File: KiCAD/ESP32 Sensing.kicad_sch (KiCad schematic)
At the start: 33 parts, among them J2 Ext Battery 3.3V, J3 Sensor, J4 Thermistor, J5 Light Detect, J6 MICRO-B USB, Q1 MMBT3904, Q2 NDS356AP, SW1 PTS526_SK15_SMTR2_LFS, U1 ESP32-WROOM-32, U2 AMS1117-3.3

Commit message: Documentation update
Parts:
- R13: footprint (none) -> Resistor_SMD:R_0805_2012Metric_Pad1.20x1.40mm_HandSolder
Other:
- note added: "Generic Sensor Input"
- note added: "Heat Sensor"
- note added: "Light Sensor"
- note added: "Voltage Monitoring"
- note removed: "Battery Voltage Monitoring"
- note removed: "Light Detector"
- note removed: "Sensor Input"
- note removed: "Thermistor"
- company: (none) -> Guy Turcotte
- title: (none) -> ESP32 Sensing Device
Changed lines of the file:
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@@
 (kicad_sch (version 20211123) (generator eeschema)
   (paper "A4")
+  (title_block
+    (title "ESP32 Sensing Device")
+    (date "2022-03-23")
+    (rev "1.0")
+    (company "Guy Turcotte")
+  )
   (junction (at 49.53 109.22) (diameter 0) (color 0 0 0 0)
   )
@@
     (stroke (width 0) (type default) (color 0 0 0 0))
   )
-  (text "Thermistor" (at 26.67 153.67 0)
+  (text "Heat Sensor" (at 26.67 153.67 0)
     (effects (font (size 1.27 1.27)) (justify left bottom))
   )
-  (text "Battery Voltage Monitoring" (at 185.42 86.36 0)
+  (text "Voltage Monitoring" (at 185.42 86.36 0)
     (effects (font (size 1.27 1.27)) (justify left bottom))
   )
@@
     (effects (font (size 1.27 1.27)) (justify left bottom))
   )
-  (text "Sensor Input" (at 185.42 35.56 0)
+  (text "Generic Sensor Input" (at 185.42 35.56 0)
     (effects (font (size 1.27 1.27)) (justify left bottom))
   )
@@
     (effects (font (size 1.27 1.27)) (justify left bottom))
   )
-  (text "Light Detector" (at 68.58 153.67 0)
+  (text "Light Sensor" (at 68.58 153.67 0)
     (effects (font (size 1.27 1.27)) (justify left bottom))
   )
@@
       (effects (font (size 1.27 1.27)) (justify left))
     )
-    (property "Footprint" "" (id 2) (at 50.292 68.58 90)
-      (effects (font (size 1.27 1.27)) hide)
-    )
+    (property "Footprint" "Resistor_SMD:R_0805_2012Metric_Pad1.20x1.40mm_HandSolder" (id 2) (at 50.292 68.58 90)
+      (effects (font (size 1.27 1.27)) hide)
+    )

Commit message: Some symbol adjustments
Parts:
- removed Q2: NDS356AP, Package_TO_SOT_SMD:SOT-23, symbol Transistor_FET:BSS84
- added Q2: (no value), Package_TO_SOT_SMD:SOT-23, symbol ESP32 Sensing:NDS356AP
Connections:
- net +3V3: now also Q2.2 (S)
- net at Q1.3 (C), R1.2: now also Q2.1 (G)
- net at R3.2: now also Q2.3 (D)
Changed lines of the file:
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@@
     (pin "2")
-  )
-  (symbol (lib_id "Transistor_FET:BSS84") (at 217.17 102.87 270) (mirror x) (unit 1)
-    (in_bom yes) (on_board yes) (fields_autoplaced)
-    (property "Reference" "Q2" (id 0) (at 217.17 92.71 90))
-    (property "Value" "NDS356AP" (id 1) (at 217.17 95.25 90))
-    (property "Footprint" "Package_TO_SOT_SMD:SOT-23" (id 2) (at 215.265 97.79 0)
-      (effects (font (size 1.27 1.27) italic) (justify left) hide)
-    )
-    (property "Datasheet" "http://assets.nexperia.com/documents/data-sheet/BSS84.pdf" (id 3) (at 217.17 102.87 0)
-      (effects (font (size 1.27 1.27)) (justify left) hide)
-    )
-    (pin "1")
-    (pin "2")
-    (pin "3")
   )
   (symbol (lib_id "power:GND") (at 226.06 69.85 0) (unit 1)
@@
     (pin "2")
   )
+  (symbol (lib_id "ESP32 Sensing:NDS356AP") (at 217.17 100.33 270) (mirror x) (unit 1)
+    (in_bom yes) (on_board yes) (fields_autoplaced)
+    (property "Reference" "Q2" (id 0) (at 217.17 92.71 90))
+    (property "Value" "" (id 1) (at 217.17 95.25 90))
+    (property "Footprint" "Package_TO_SOT_SMD:SOT-23" (id 2) (at 205.74 100.33 0)
+      (effects (font (size 1.27 1.27)) hide)
+    )
+    (property "Datasheet" "https://rocelec.widen.net/view/pdf/qv8gjztlsc/ONSM-S-A0003585169-1.pdf?t.download=true&u=5oefqw" (id 3) (at 203.2 99.06 0)
+      (effects (font (size 1.27 1.27)) hide)
+    )
+    (pin "1")
+    (pin "2")
+    (pin "3")
+  )
   (sheet_instances
     (path "/" (page "1"))
@@
       (reference "Q1") (unit 1) (value "MMBT3904") (footprint "Package_TO_SOT_SMD:SOT-23")
     )
-    (path "/5e813023-f164-4a19-bc58-3eafdf40bdee"
+    (path "/f4d07452-5838-44e6-b966-b49f14e25425"
       (reference "Q2") (unit 1) (value "NDS356AP") (footprint "Package_TO_SOT_SMD:SOT-23")
     )

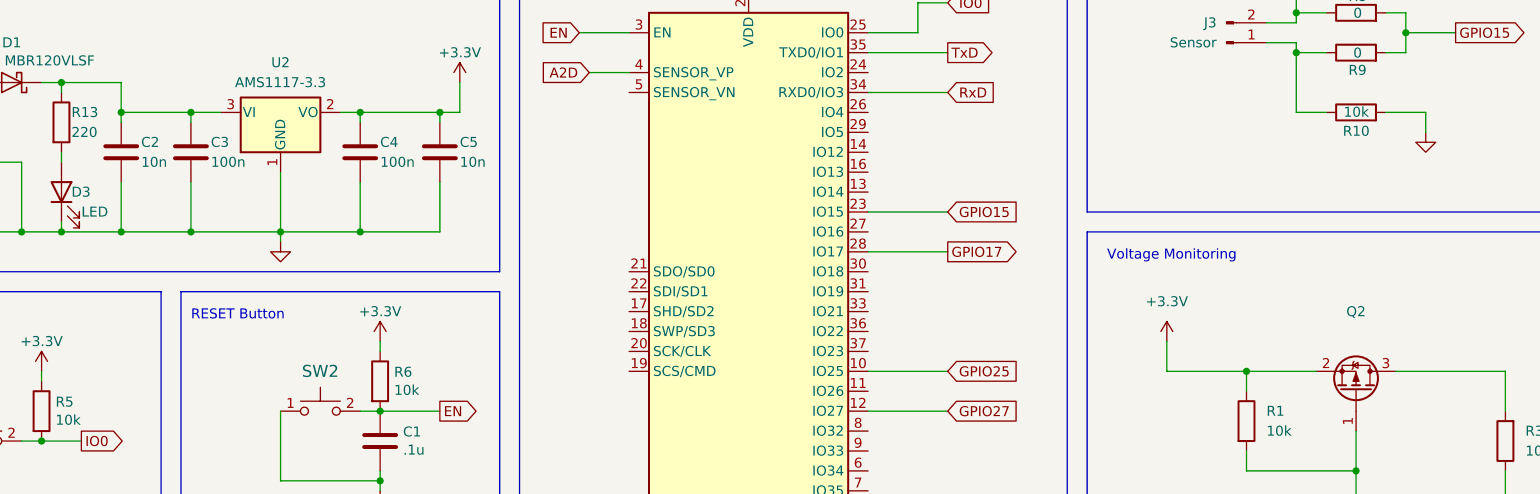
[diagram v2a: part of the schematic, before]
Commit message: Modified linear regulator  capacitor values
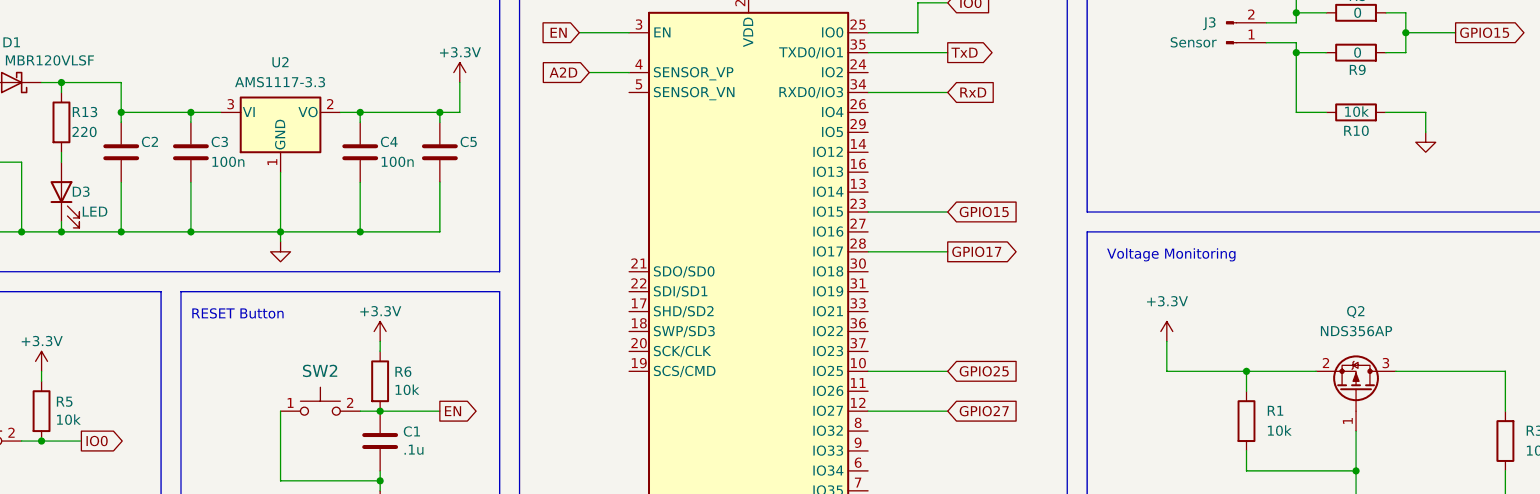
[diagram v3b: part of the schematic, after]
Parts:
- C2: value 10n -> (none); footprint Capacitor_SMD:C_0805_2012Metric_Pad1.18x1.45mm_HandSolder -> (none)
- C5: value 10n -> (none)
- Q2: value (none) -> NDS356AP
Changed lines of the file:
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@@
       (effects (font (size 1.27 1.27)) (justify left))
     )
-    (property "Value" "10n" (id 1) (at 62.23 73.66 0)
-      (effects (font (size 1.27 1.27)) (justify left))
-    )
-    (property "Footprint" "Capacitor_SMD:C_0805_2012Metric_Pad1.18x1.45mm_HandSolder" (id 2) (at 60.6552 76.2 0)
+    (property "Value" "" (id 1) (at 62.23 73.66 0)
+      (effects (font (size 1.27 1.27)) (justify left))
+    )
+    (property "Footprint" "" (id 2) (at 60.6552 76.2 0)
       (effects (font (size 1.27 1.27)) hide)
     )
@@
       (effects (font (size 1.27 1.27)) (justify left))
     )
-    (property "Value" "10n" (id 1) (at 102.87 73.66 0)
+    (property "Value" "" (id 1) (at 102.87 73.66 0)
       (effects (font (size 1.27 1.27)) (justify left))
     )
@@
     (in_bom yes) (on_board yes) (fields_autoplaced)
     (property "Reference" "Q2" (id 0) (at 217.17 92.71 90))
-    (property "Value" "" (id 1) (at 217.17 95.25 90))
+    (property "Value" "NDS356AP" (id 1) (at 217.17 95.25 90))
     (property "Footprint" "Package_TO_SOT_SMD:SOT-23" (id 2) (at 205.74 100.33 0)
       (effects (font (size 1.27 1.27)) hide)
@@
     )
     (path "/3322442e-6e2b-4aec-8963-f9711a4d7d5a"
-      (reference "C2") (unit 1) (value "10n") (footprint "Capacitor_SMD:C_0805_2012Metric_Pad1.18x1.45mm_HandSolder")
+      (reference "C2") (unit 1) (value "10u") (footprint "Capacitor_SMD:C_0805_2012Metric_Pad1.18x1.45mm_HandSolder")
     )
     (path "/ad0f22cf-16aa-4712-8b8d-6d4df83357d3"
@@
     )
     (path "/f3edeb31-1206-44d1-a81c-d4b62d24bf49"
-      (reference "C5") (unit 1) (value "10n") (footprint "Capacitor_SMD:C_0805_2012Metric_Pad1.18x1.45mm_HandSolder")
+      (reference "C5") (unit 1) (value "10u") (footprint "Capacitor_SMD:C_0805_2012Metric_Pad1.18x1.45mm_HandSolder")
     )
     (path "/2af885a8-38bb-4e65-b90c-6c0a01eeb3bb"
